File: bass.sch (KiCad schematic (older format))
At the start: 13 parts, among them J101 Output, J102 Input, J103 Jack-DC, U101 TL074, U102 TL074

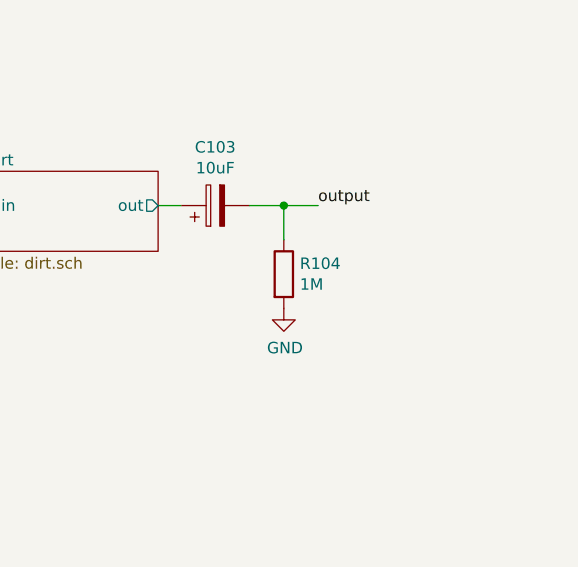
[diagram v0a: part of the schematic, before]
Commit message: Add dirt section, some controls
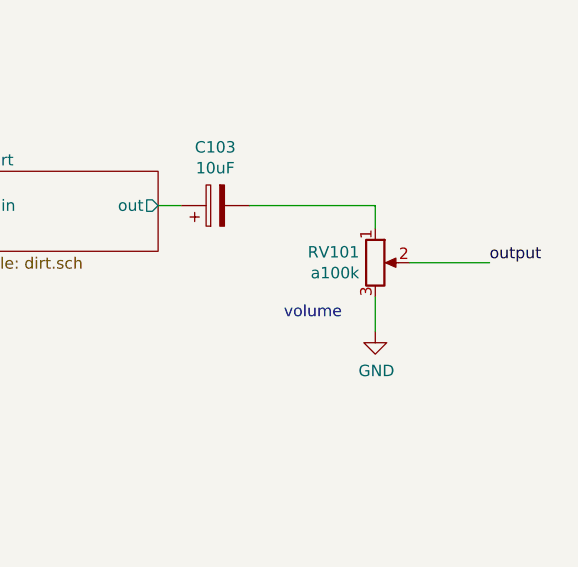
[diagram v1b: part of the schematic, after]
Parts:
- removed R104: 1M, symbol Device:R
- added RV101: a100k, symbol Device:R_POT
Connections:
- net GND: now also RV101.3
- net output: now also RV101.2; no longer C103.2
- new net: C103.2, RV101.1
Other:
- note added: "volume"
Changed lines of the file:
@@
-$EndComp
-$Comp
-L Device:R R104
-U 1 1 5F4AB8C1
-P 6400 4050
-F 0 "R104" H 6470 4096 50  0000 L CNN
-F 1 "1M" H 6470 4005 50  0000 L CNN
-F 2 "" V 6330 4050 50  0001 C CNN
-F 3 "~" H 6400 4050 50  0001 C CNN
-	1    6400 4050
-	1    0    0    -1
-$EndComp
-Wire Wire Line
-	6400 3900 6400 3750
-Wire Wire Line
-	6400 3750 6250 3750
-$Comp
-L power:GND #PWR0105
-U 1 1 5F4ACAFF
-P 6400 4200
-F 0 "#PWR0105" H 6400 3950 50  0001 C CNN
-F 1 "GND" H 6405 4027 50  0000 C CNN
-F 2 "" H 6400 4200 50  0001 C CNN
-F 3 "" H 6400 4200 50  0001 C CNN
-	1    6400 4200
-	1    0    0    -1
 $EndComp
 $Comp
@@
 Connection ~ 3700 3750
 Wire Wire Line
-	6400 3750 6550 3750
-Connection ~ 6400 3750
-Wire Wire Line
 	1850 3650 1700 3650
 Wire Wire Line
@@
 Text Label 1500 1800 0    50   ~ 0
 output
-Text Label 6550 3750 0    50   ~ 0
+Text Label 7300 4000 0    50   ~ 0
 output
 Text Label 1700 3650 2    50   ~ 0
@@
 Wire Wire Line
 	4800 3750 5100 3750
+$Comp
+L Device:R_POT RV101
+U 1 1 5F4D1371
+P 6800 4000
+F 0 "RV101" H 6730 4046 50  0000 R CNN
+F 1 "a100k" H 6730 3955 50  0000 R CNN
+F 2 "" H 6800 4000 50  0001 C CNN
+F 3 "~" H 6800 4000 50  0001 C CNN
+	1    6800 4000
+	1    0    0    -1
+$EndComp
+$Comp
+L power:GND #PWR0105
+U 1 1 5F4D1C33
+P 6800 4300
+F 0 "#PWR0105" H 6800 4050 50  0001 C CNN
+F 1 "GND" H 6805 4127 50  0000 C CNN
+F 2 "" H 6800 4300 50  0001 C CNN
+F 3 "" H 6800 4300 50  0001 C CNN
+	1    6800 4300
+	1    0    0    -1
+$EndComp
+Wire Wire Line
+	6800 4300 6800 4150
+Wire Wire Line
+	6800 3850 6800 3750
+Wire Wire Line
+	6250 3750 6800 3750
+Wire Wire Line
+	6950 4000 7300 4000
+Text Notes 6400 4250 0    50   ~ 0
+volume
 $EndSCHEMATC
